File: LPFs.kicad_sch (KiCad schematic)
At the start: 21 parts

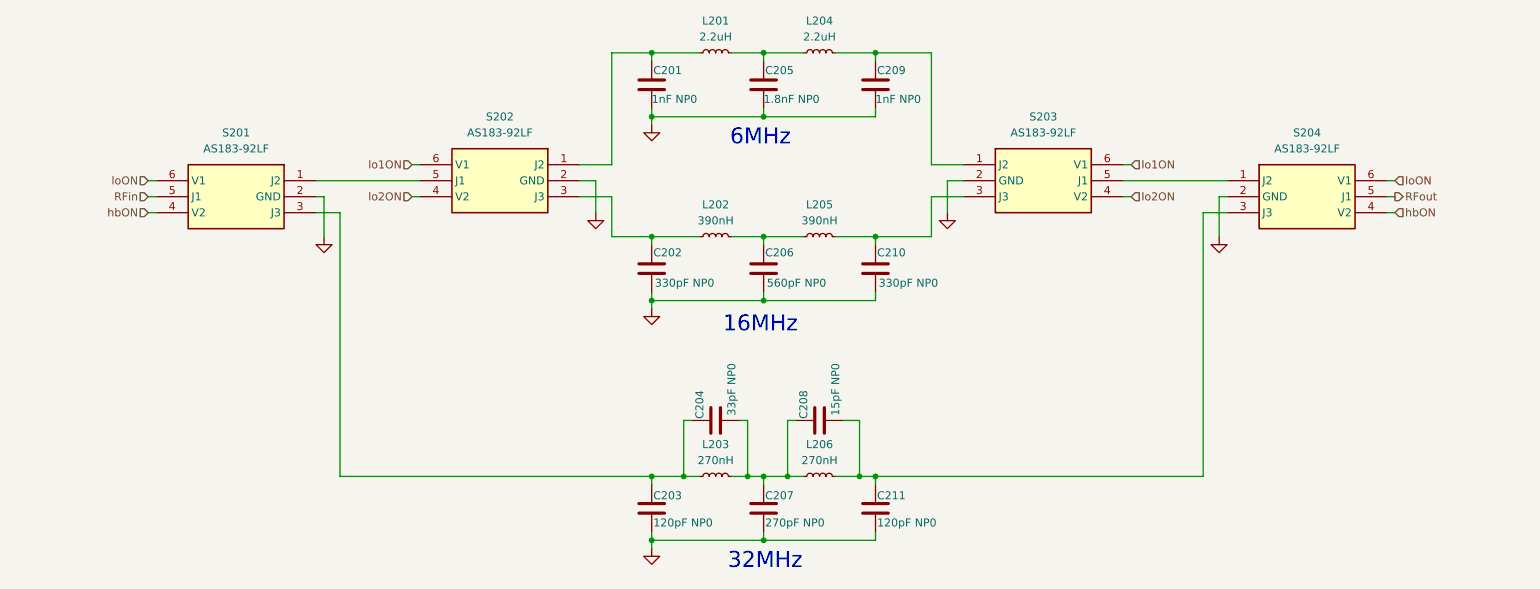
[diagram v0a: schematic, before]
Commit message: Fix filters for proper response. Now we have FPGA + ESP32S3.
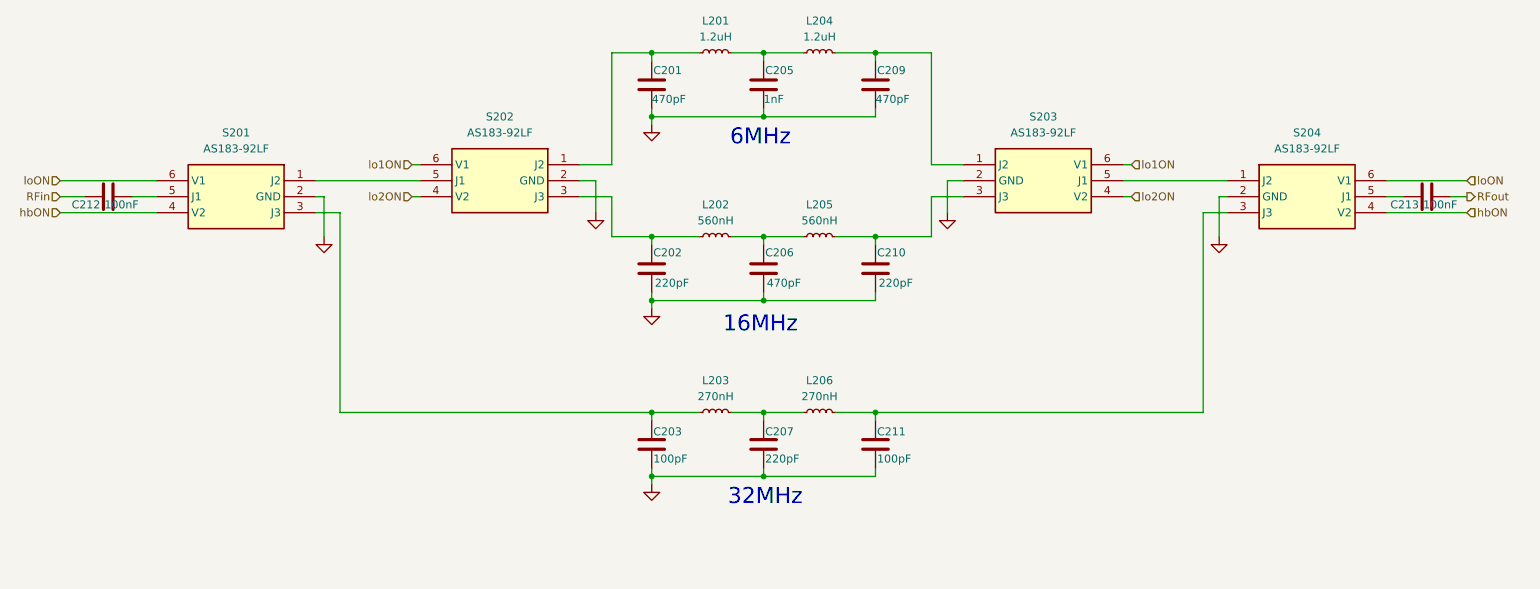
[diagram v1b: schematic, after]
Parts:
- removed C204: 33pF NP0, Capacitor_SMD:C_0603_1608Metric, symbol Device:C
- removed C208: 15pF NP0, Capacitor_SMD:C_0603_1608Metric, symbol Device:C
- added C212, C213: 100nF, Capacitor_SMD:C_0603_1608Metric, symbol Device:C
- C201, C209: value 1nF NP0 -> 470pF
- C202, C210: value 330pF NP0 -> 220pF
- C203, C211: value 120pF NP0 -> 100pF
- C205: value 1.8nF NP0 -> 1nF
- C206: value 560pF NP0 -> 470pF
- C207: value 270pF NP0 -> 220pF
- L201, L204: value 2.2uH -> 1.2uH
- L202, L205: value 390nH -> 560nH
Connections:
- net RFin: now also C212.1; no longer S201.5 (J1)
- net RFout: now also C213.2; no longer S204.5 (J1)
- new net: C213.1, S204.5 (J1)
- new net: C212.2, S201.5 (J1)
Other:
- moved on the sheet: C203, C207, C211, L203, L206

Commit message: Well it is routed and passes DRC
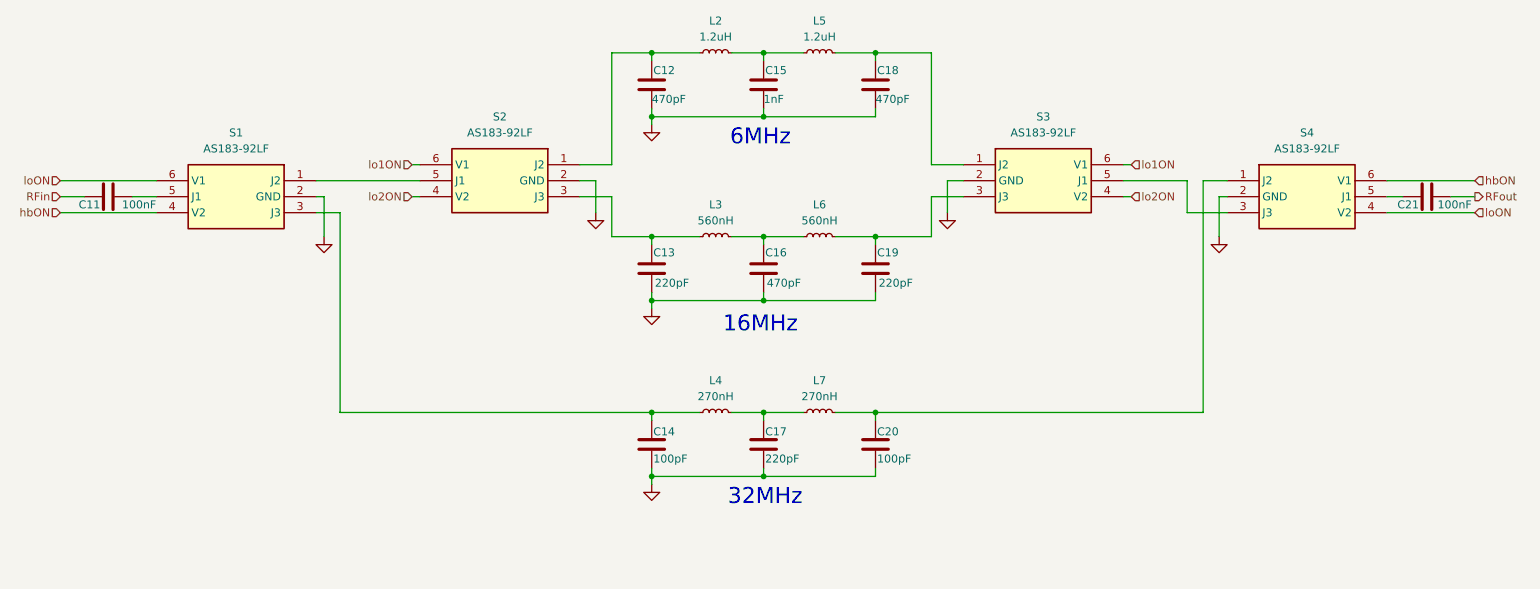
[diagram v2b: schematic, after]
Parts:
- renumbered C212 to C11, C201 to C12, C202 to C13, C203 to C14, C205 to C15, C206 to C16, C207 to C17, C209 to C18, C210 to C19, C211 to C20, C213 to C21, L201 to L2, L202 to L3, L203 to L4, L204 to L5, L205 to L6, L206 to L7, S201 to S1, S202 to S2, S203 to S3, S204 to S4
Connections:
- net hbON: now also S4.6 (V1); no longer S4.4 (V2)
- net loON: now also S4.4 (V2); no longer S4.6 (V1)
- net at S4.1 (J2): now also C20.1, L7.2; no longer S3.5 (J1)
- new net: S3.5 (J1), S4.3 (J3)

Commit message: Minor tweaks after submitting 001 build to pcbway
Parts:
- L2, L5: LCSC (none) -> C46470448; MFG Coilcraft -> (none); MPN 1008LS-222 -> (none); Manufacturer_Name (none) -> Coilcraft; Mouser Part Number (none) -> 1008LS-222
- L3, L6: LCSC (none) -> C20417044; MFG Coilcraft -> (none); MPN 0805CS-391 -> (none); Manufacturer_Name (none) -> Coilcraft; Mouser Part Number (none) -> 0805CS-391XGLC
- L4, L7: LCSC (none) -> C20623520; MFG Coilcraft -> (none); MPN 0805CS-271 -> (none); Manufacturer_Name (none) -> Coilcraft; Mouser Part Number (none) -> 0805CS-271 XGLC
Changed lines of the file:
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@@
 			)
 		)
-		(property "MFG" "Coilcraft"
+		(property "MFG" ""
 			(at 132.08 34.29 90)
 			(effects
@@
 			)
 		)
-		(property "MPN" "1008LS-222"
+		(property "MPN" ""
 			(at 132.08 34.29 90)
 			(effects
@@
 			)
 		)
-		(property "LCSC" ""
+		(property "LCSC" "C46470448"
+			(at 132.08 34.29 90)
+			(effects
+				(font
+					(size 1.27 1.27)
+				)
+				(hide yes)
+			)
+		)
+		(property "Manufacturer_Name" "Coilcraft"
+			(at 132.08 34.29 90)
+			(effects
+				(font
+					(size 1.27 1.27)
+				)
+				(hide yes)
+			)
+		)
+		(property "Mouser Part Number" "1008LS-222"
 			(at 132.08 34.29 90)
 			(effects
@@
 			)
 		)
-		(property "MFG" "Coilcraft"
+		(property "MFG" ""
 			(at 148.59 34.29 90)
 			(effects
@@
 			)
 		)
-		(property "MPN" "1008LS-222"
+		(property "MPN" ""
 			(at 148.59 34.29 90)
 			(effects
@@
 			)
 		)
-		(property "LCSC" ""
+		(property "LCSC" "C46470448"
+			(at 148.59 34.29 90)
+			(effects
+				(font
+					(size 1.27 1.27)
+				)
+				(hide yes)
+			)
+		)
+		(property "Manufacturer_Name" "Coilcraft"
+			(at 148.59 34.29 90)
+			(effects
+				(font
+					(size 1.27 1.27)
+				)
+				(hide yes)
+			)
+		)
+		(property "Mouser Part Number" "1008LS-222"
 			(at 148.59 34.29 90)
 			(effects
@@
 			)
 		)
-		(property "MFG" "Coilcraft"
+		(property "MFG" ""
 			(at 148.59 63.5 90)
 			(effects
@@
 			)
 		)
-		(property "MPN" "0805CS-391"
+		(property "MPN" ""
 			(at 148.59 63.5 90)
 			(effects
@@
 			)
 		)
-		(property "LCSC" ""
+		(property "LCSC" "C20417044"
+			(at 148.59 63.5 90)
+			(effects
+				(font
+					(size 1.27 1.27)
+				)
+				(hide yes)
+			)
+		)
+		(property "Manufacturer_Name" "Coilcraft"
+			(at 148.59 63.5 90)
+			(effects
+				(font
+					(size 1.27 1.27)
+				)
+				(hide yes)
+			)
+		)
+		(property "Mouser Part Number" "0805CS-391XGLC"
 			(at 148.59 63.5 90)
 			(effects
@@
 			)
 		)
-		(property "MFG" "Coilcraft"
+		(property "MFG" ""
 			(at 148.59 91.44 90)
 			(effects
@@
 			)
 		)
-		(property "MPN" "0805CS-271"
+		(property "MPN" ""
 			(at 148.59 91.44 90)
 			(effects
@@
 			)
 		)
-		(property "LCSC" ""
+		(property "LCSC" "C20623520"
+			(at 148.59 91.44 90)
+			(effects
+				(font
+					(size 1.27 1.27)
+				)
+				(hide yes)
+			)
+		)
+		(property "Manufacturer_Name" "Coilcraft"
+			(at 148.59 91.44 90)
+			(effects
+				(font
+					(size 1.27 1.27)
+				)
+				(hide yes)
+			)
+		)
+		(property "Mouser Part Number" "0805CS-271 XGLC"
 			(at 148.59 91.44 90)
 			(effects
@@
 			)
 		)
-		(property "MFG" "Coilcraft"
+		(property "MFG" ""
 			(at 132.08 91.44 90)
 			(effects
@@
 			)
 		)
-		(property "MPN" "0805CS-271"
+		(property "MPN" ""
 			(at 132.08 91.44 90)
 			(effects
@@
 			)
 		)
-		(property "LCSC" ""
+		(property "LCSC" "C20623520"
+			(at 132.08 91.44 90)
+			(effects
+				(font
+					(size 1.27 1.27)
+				)
+				(hide yes)
+			)
+		)
+		(property "Manufacturer_Name" "Coilcraft"
+			(at 132.08 91.44 90)
+			(effects
+				(font
+					(size 1.27 1.27)
+				)
+				(hide yes)
+			)
+		)
+		(property "Mouser Part Number" "0805CS-271 XGLC"
 			(at 132.08 91.44 90)
 			(effects
@@
 			)
 		)
-		(property "MFG" "Coilcraft"
+		(property "MFG" ""
 			(at 132.08 63.5 90)
 			(effects
@@
 			)
 		)
-		(property "MPN" "0805CS-391"
+		(property "MPN" ""
 			(at 132.08 63.5 90)
 			(effects
@@
 			)
 		)
-		(property "LCSC" ""
+		(property "LCSC" "C20417044"
 			(at 132.08 63.5 90)
 			(effects
+				(font
+					(size 1.27 1.27)
+				)
+				(hide yes)
+			)
+		)
+		(property "Manufacturer_Name" "Coilcraft"
+			(at 132.08 63.5 90)
+			(effects
+				(font
+					(size 1.27 1.27)
+				)
+				(hide yes)
+			)
+		)
+		(property "Mouser Part Number" "0805CS-391XGLC"
+			(at 132.08 63.5 90)
+			(effects

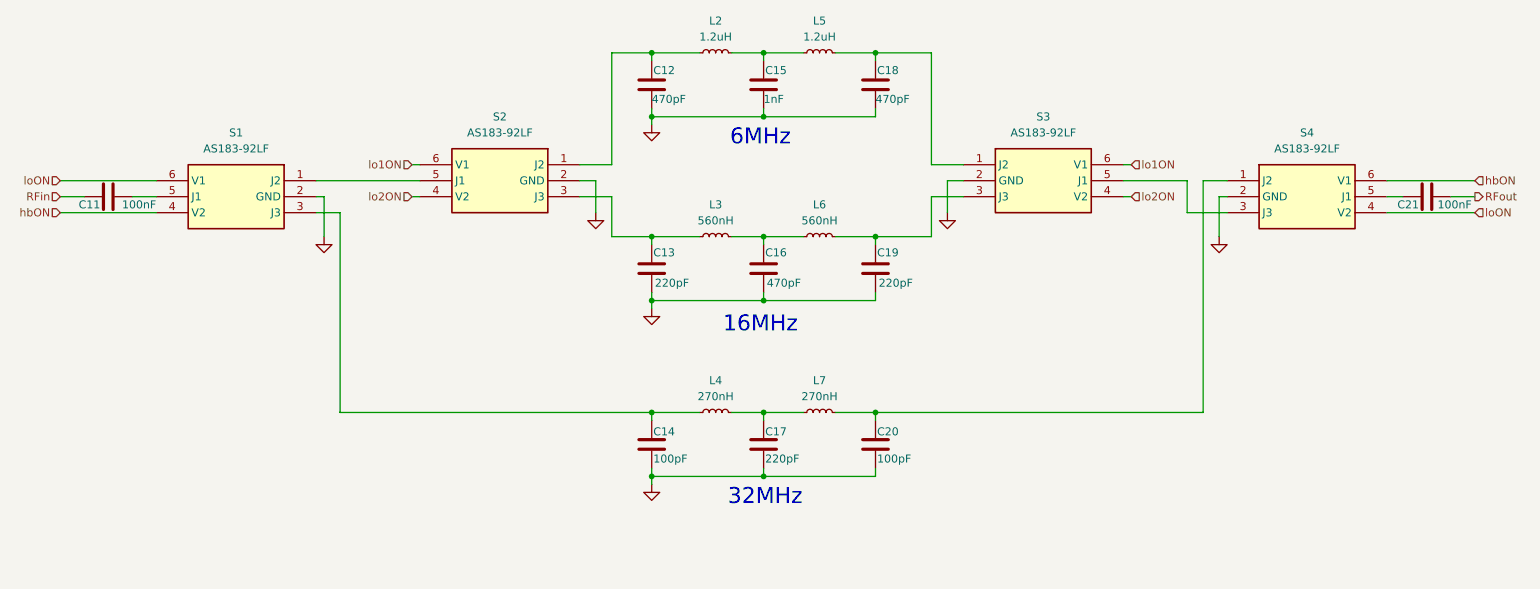
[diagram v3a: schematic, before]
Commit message: Submitted to PCBway (I had to update BOM after oops)
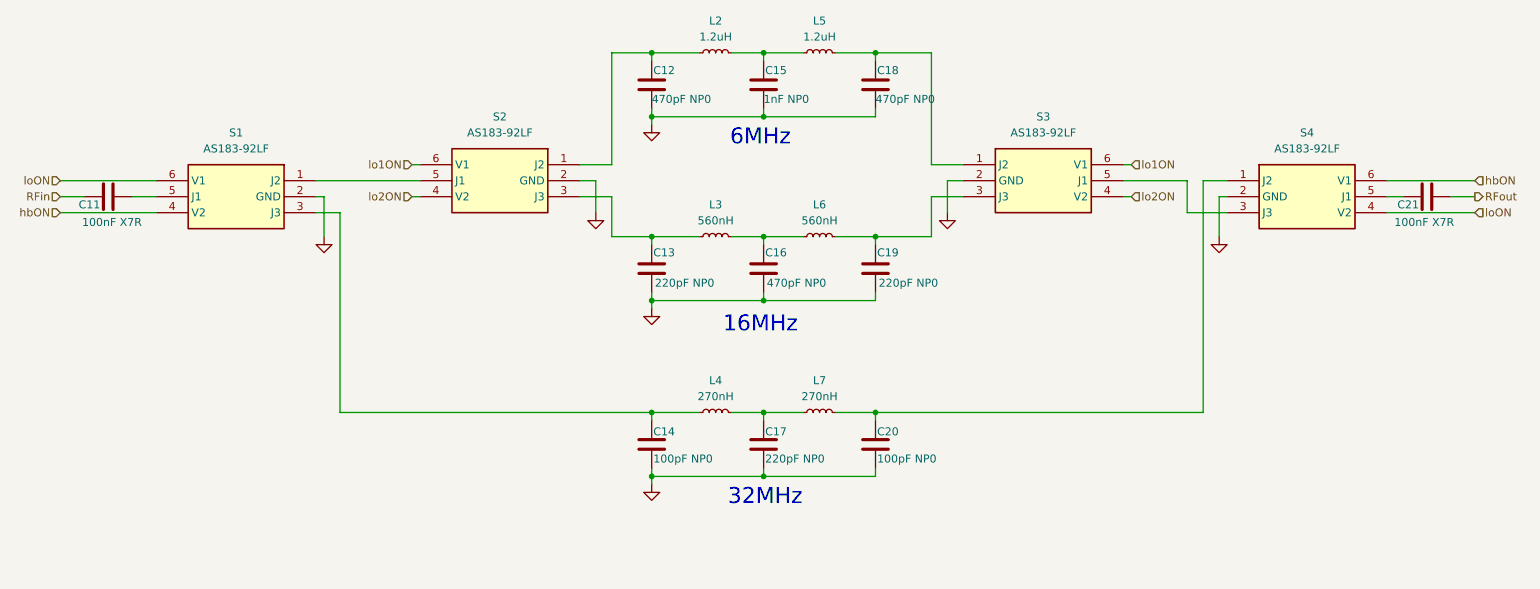
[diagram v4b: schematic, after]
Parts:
- C11, C21: value 100nF -> 100nF X7R; LCSC (none) -> C14663
- C12, C16, C18: value 470pF -> 470pF NP0; LCSC (none) -> C106211
- C13, C17, C19: value 220pF -> 220pF NP0; LCSC (none) -> C106210
- C14, C20: value 100pF -> 100pF NP0; LCSC (none) -> C14665
- C15: value 1nF -> 1nF NP0; LCSC (none) -> C1588
- S1, S2, S3, S4: LCSC (none) -> C2654768
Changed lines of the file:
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@@
 			)
 		)
-		(property "Value" "470pF"
+		(property "Value" "470pF NP0"
 			(at 157.48 41.656 0)
 			(effects
@@
 			)
 		)
-		(property "LCSC" ""
+		(property "LCSC" "C106211"
 			(at 157.48 39.37 0)
 			(effects
@@
 			)
 		)
-		(property "LCSC" ""
+		(property "LCSC" "C2654768"
 			(at 213.36 54.61 0)
 			(effects
@@
 			)
 		)
-		(property "Value" "100pF"
+		(property "Value" "100pF NP0"
 			(at 122.174 98.806 0)
 			(effects
@@
 			)
 		)
-		(property "LCSC" ""
+		(property "LCSC" "C14665"
 			(at 121.92 96.52 0)
 			(effects
@@
 			)
 		)
-		(property "LCSC" ""
+		(property "LCSC" "C2654768"
 			(at 171.45 52.07 0)
 			(effects
@@
 			)
 		)
-		(property "Value" "100nF"
-			(at 252.222 58.42 90)
+		(property "Value" "100nF X7R"
+			(at 249.428 61.214 90)
 			(effects
 				(font
@@
 			)
 		)
-		(property "LCSC" ""
+		(property "LCSC" "C14663"
 			(at 245.11 57.15 90)
 			(effects
@@
 			)
 		)
-		(property "Value" "100pF"
+		(property "Value" "100pF NP0"
 			(at 157.734 98.806 0)
 			(effects
@@
 			)
 		)
-		(property "LCSC" ""
+		(property "LCSC" "C14665"
 			(at 157.48 96.52 0)
 			(effects
@@
 			)
 		)
-		(property "Value" "470pF"
+		(property "Value" "470pF NP0"
 			(at 140.208 70.866 0)
 			(effects
@@
 			)
 		)
-		(property "LCSC" ""
+		(property "LCSC" "C106211"
 			(at 139.7 68.58 0)
 			(effects
@@
 			)
 		)
-		(property "LCSC" ""
+		(property "LCSC" "C2654768"
 			(at 68.58 54.61 0)
 			(effects
@@
 			)
 		)
-		(property "Value" "1nF"
+		(property "Value" "1nF NP0"
 			(at 139.7 41.656 0)
 			(effects
@@
 			)
 		)
-		(property "LCSC" ""
+		(property "LCSC" "C1588"
 			(at 139.7 39.37 0)
 			(effects
@@
 			)
 		)
-		(property "Value" "100nF"
-			(at 43.18 58.42 90)
+		(property "Value" "100nF X7R"
+			(at 40.894 61.214 90)
 			(effects
 				(font
@@
 			)
 		)
-		(property "LCSC" ""
+		(property "LCSC" "C14663"
 			(at 35.56 57.15 90)
 			(effects
@@
 			)
 		)
-		(property "Value" "220pF"
+		(property "Value" "220pF NP0"
 			(at 122.428 70.866 0)
 			(effects
@@
 			)
 		)
-		(property "LCSC" ""
+		(property "LCSC" "C106210"
 			(at 121.92 68.58 0)
 			(effects
@@
 			)
 		)
-		(property "Value" "220pF"
+		(property "Value" "220pF NP0"
 			(at 157.988 70.866 0)
 			(effects
@@
 			)
 		)
-		(property "LCSC" ""
+		(property "LCSC" "C106210"
 			(at 157.48 68.58 0)
 			(effects
@@
 			)
 		)
-		(property "Value" "220pF"
+		(property "Value" "220pF NP0"
 			(at 139.954 98.806 0)
 			(effects
@@
 			)
 		)
-		(property "LCSC" ""
+		(property "LCSC" "C106210"
 			(at 139.7 96.52 0)
 			(effects
@@
 			)
 		)
-		(property "Value" "470pF"
+		(property "Value" "470pF NP0"
 			(at 121.92 41.656 0)
 			(effects
@@
 			)
 		)
-		(property "LCSC" ""
+		(property "LCSC" "C106211"
 			(at 121.92 39.37 0)
 			(effects
@@
 			)
 		)
-		(property "LCSC" ""
+		(property "LCSC" "C2654768"
 			(at 110.49 52.07 0)
 			(effects

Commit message: Cleanup. Better USB diff pair with 0ohm and TVS as recommended. Return to rectangular outline and even smaller. Mounting holes are consistently placed relative to board corners.
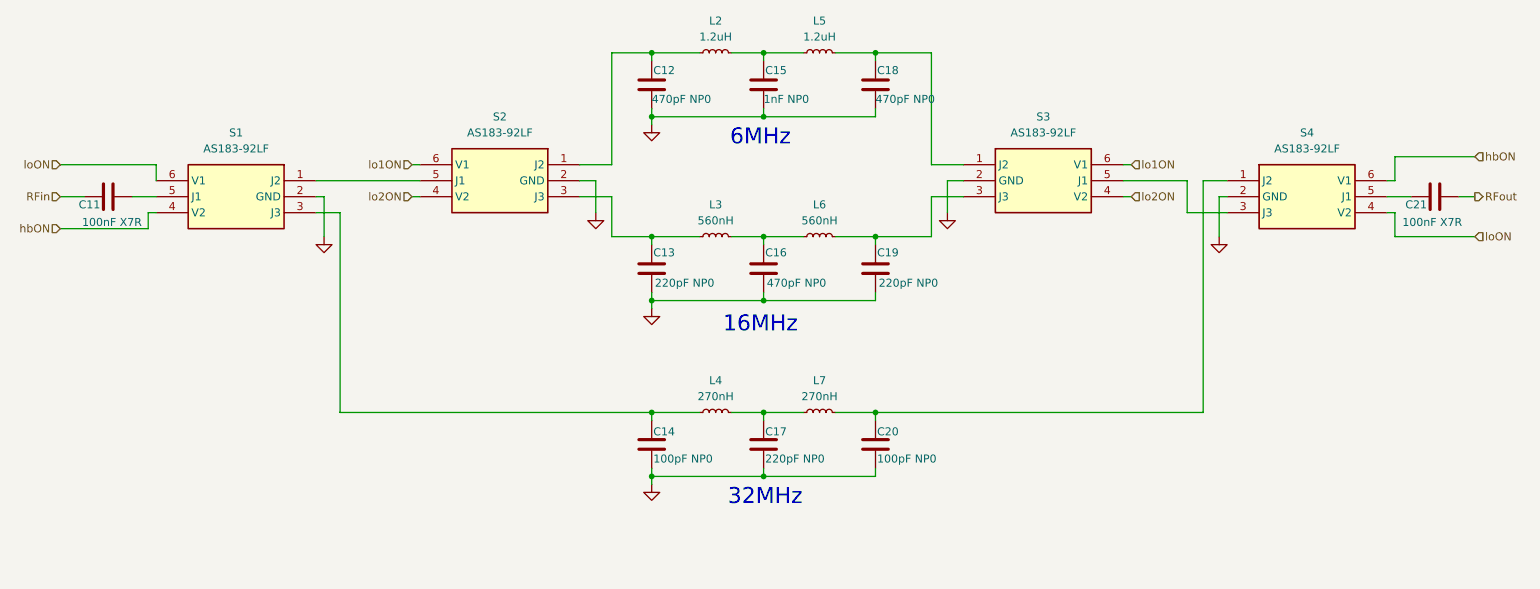
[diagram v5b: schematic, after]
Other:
- moved on the sheet: C21
